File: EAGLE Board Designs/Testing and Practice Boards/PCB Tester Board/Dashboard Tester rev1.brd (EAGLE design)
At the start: 160 x 100 mm, 26 parts, among them J1 CONNECTOR-CAN_NF_T_V_BLACK, J2 CONNECTOR-6_NF_T_V_BLACK, J3 CONNECTOR-8_NF_T_V_BLACK, Q1 TRANSISTOR_N_MOS_PMV15ENEA, Q10 TRANSISTOR_N_MOS_PMV15ENEA, Q11 TRANSISTOR_P_MOS_SOT23_SI2369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, Q2 TRANSISTOR_N_MOS_PMV15ENEA, Q3 TRANSISTOR_N_MOS_PMV15ENEA, Q4 TRANSISTOR_N_MOS_PMV15ENEA, Q5 TRANSISTOR_N_MOS_PMV15ENEA, Q6 TRANSISTOR_N_MOS_PMV15ENEA, Q7 TRANSISTOR_P_MOS_SOT23_SI2369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, Q8 TRANSISTOR_N_MOS_PMV15ENEA, Q9 TRANSISTOR_P_MOS_SOT23_SI2369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, U1 TEENSY_3.5, U2 CAN_TRANSCIEVER_TCAN1051HQV-Q1, U3 VOLTAGE_REGULATOR__5V

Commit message: Merge in master to update files
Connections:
- net VIO renamed +3V3
- removed net IN: U3.1
- removed net OUT: U3.3
- removed net VDD: U2.3
- removed net VIN: U1.VIN
- new net +5V: U1.VIN, U2.3, U3.3
- new net CANH: J1.4, U2.7
- new net CANL: J1.3, U2.6
- new net N$20: U1.D3, U2.1
- new net N$23: U1.D4, U2.4
- net +12V: now also U3.1
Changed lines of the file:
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@@
 </elements>
 <signals>
-<signal name="VIN">
-<contactref element="U1" pad="VIN"/>
-</signal>
 <signal name="AGND">
 <contactref element="U1" pad="AGND/GND"/>
@@
 <wire x1="-57.13" y1="6.35" x2="-30.48" y2="38.1" width="0" layer="19" extent="1-1"/>
 </signal>
-<signal name="VDD">
-<contactref element="U2" pad="3"/>
-</signal>
-<signal name="VIO">
-<contactref element="U2" pad="5"/>
-</signal>
-<signal name="IN">
-<contactref element="U3" pad="1"/>
-</signal>
-<signal name="OUT">
-<contactref element="U3" pad="3"/>
-</signal>
 <signal name="+12V">
 <contactref element="J1" pad="1"/>
@@
 <contactref element="RN6" pad="7"/>
 <contactref element="DN3" pad="3"/>
+<contactref element="U3" pad="1"/>
 <wire x1="-23.48" y1="80.33" x2="-24.8031" y2="80.33" width="0" layer="19" extent="1-1"/>
 <wire x1="-18.1102" y1="75.1967" x2="-23.48" y2="80.33" width="0" layer="19" extent="1-1"/>
+<wire x1="-21.59" y1="67.31" x2="-18.1102" y2="75.1967" width="0" layer="19" extent="1-1"/>
 <wire x1="-56.28" y1="77.1" x2="-24.8031" y2="80.33" width="0" layer="19" extent="1-1"/>
 <wire x1="-57.08" y1="77.1" x2="-56.28" y2="77.1" width="0" layer="19" extent="1-1"/>
@@
 <contactref element="Q11" pad="3"/>
 </signal>
+<signal name="+5V">
+<contactref element="U2" pad="3"/>
+<contactref element="U3" pad="3"/>
+<contactref element="U1" pad="VIN"/>
+<wire x1="-27.305" y1="63.4365" x2="-16.51" y2="67.31" width="0" layer="19" extent="1-1"/>
+<wire x1="-30.48" y1="2.54" x2="-27.305" y2="63.4365" width="0" layer="19" extent="1-1"/>
+</signal>
+<signal name="+3V3">
+<contactref element="U2" pad="5"/>
+</signal>
+<signal name="CANH">
+<contactref element="J1" pad="4"/>
+<contactref element="U2" pad="7"/>
+<wire x1="-28.575" y1="68.6435" x2="-57.13" y2="3.85" width="0" layer="19" extent="1-1"/>
+</signal>
+<signal name="CANL">
+<contactref element="J1" pad="3"/>
+<contactref element="U2" pad="6"/>
+<wire x1="-27.305" y1="68.6435" x2="-54.63" y2="3.85" width="0" layer="19" extent="1-1"/>
+</signal>
+<signal name="N$20">
+<contactref element="U2" pad="1"/>
+<contactref element="U1" pad="D3"/>
+<wire x1="-15.24" y1="12.7" x2="-29.845" y2="63.4365" width="0" layer="19" extent="1-1"/>
+</signal>
+<signal name="N$23">
+<contactref element="U1" pad="D4"/>
+<contactref element="U2" pad="4"/>
+<wire x1="-15.24" y1="15.24" x2="-26.035" y2="63.4365" width="0" layer="19" extent="1-1"/>
+</signal>
 </signals>

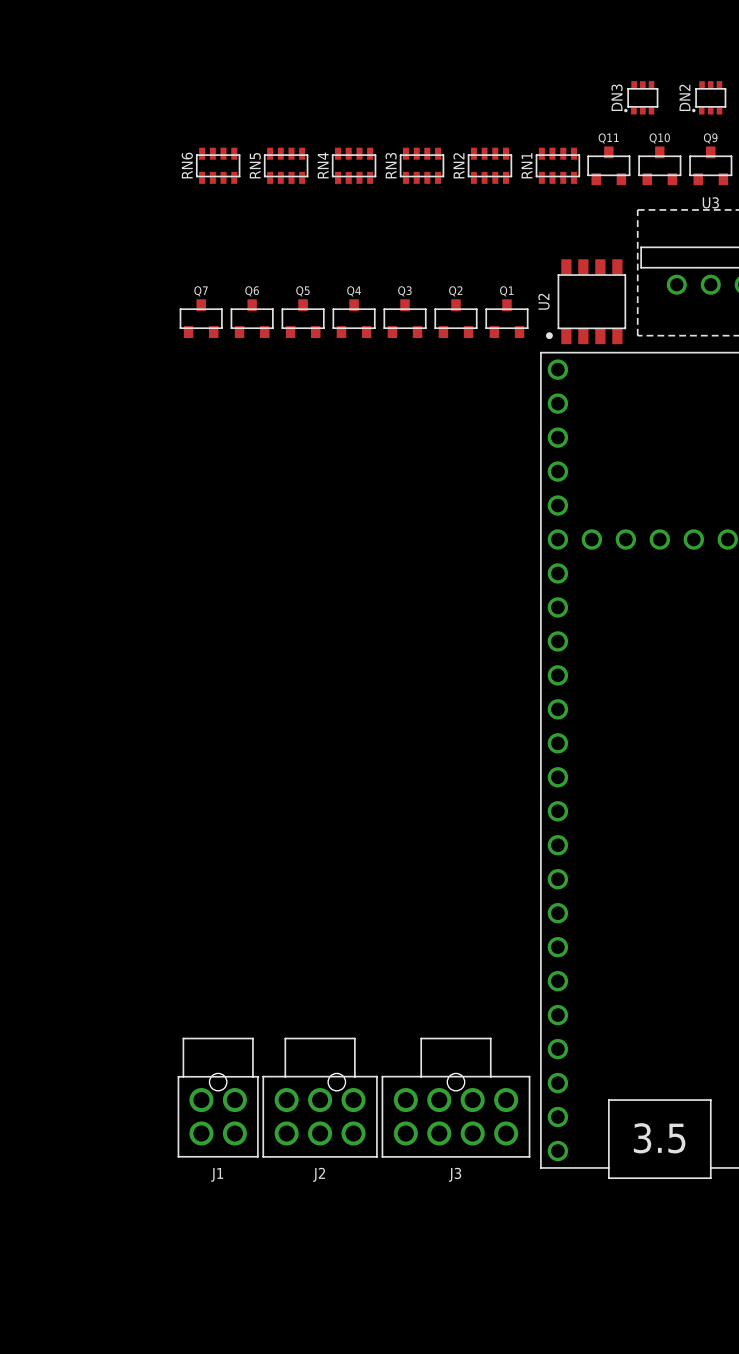
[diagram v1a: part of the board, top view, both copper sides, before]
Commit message: Ready to route except for connections to teensy
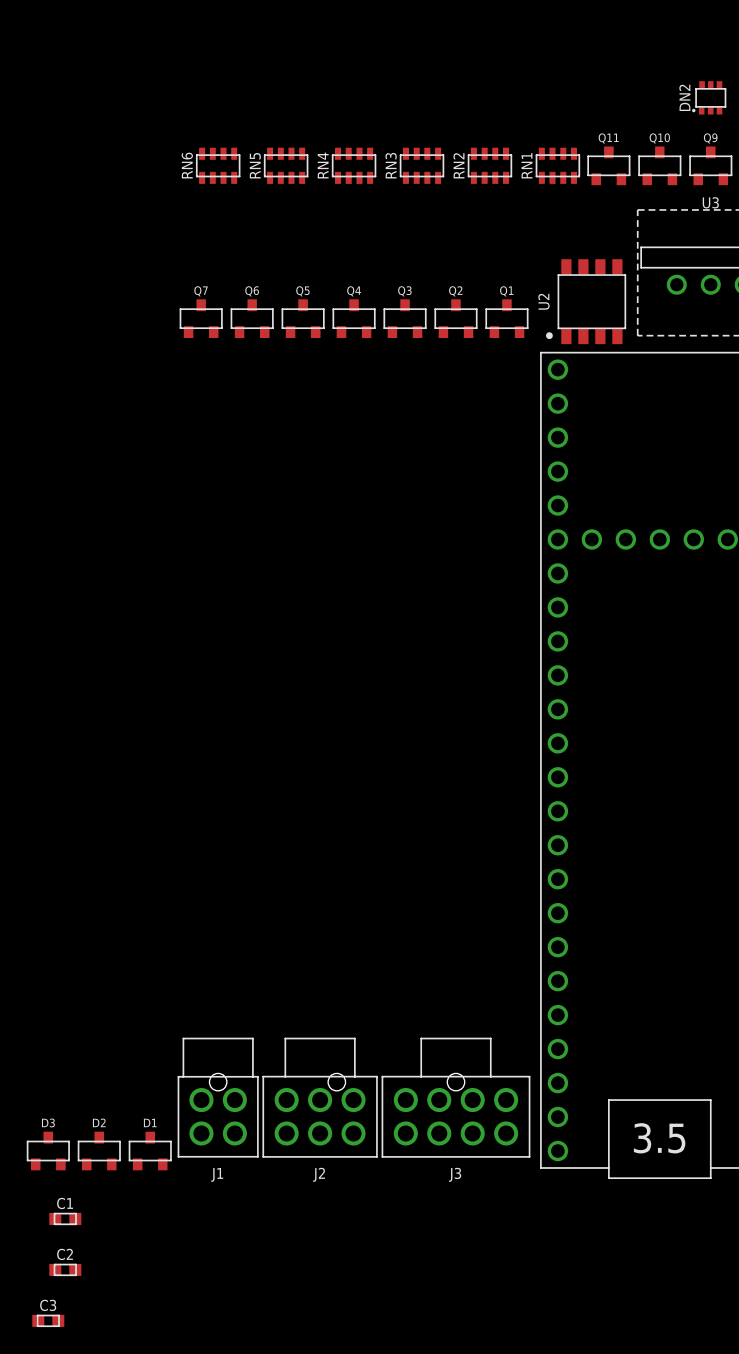
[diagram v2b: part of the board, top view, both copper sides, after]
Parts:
- removed DN3: TVS_ARRAY_16V, HyTechDevices:SOT363
- added C1: CAPACITOR_0603_25V_1UF, HyTechDevices:0603-CAP
- added C2, C3: CAPACITOR_0603_10V_1UF, HyTechDevices:0603-CAP
- added D1, D2, D3: TVS_15V, HyTechDevices:SOT-23
- U3: value VOLTAGE_REGULATOR__5V -> VOLTAGE_REGULATOR_OKI-78SR_5V
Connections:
- net N$11 renamed BTN_LC_CTRL
- net N$2 renamed BTN_MARK_CTRL
- net N$5 renamed BTN_MC_CYCLE_CTRL
- net N$7 renamed BTN_MODE_CTRL
- net N$9 renamed BTN_START_CTRL
- removed net N$25: Q5.3
- removed net N$26: Q4.3
- removed net N$27: Q3.3
- removed net N$28: Q2.3
- removed net N$29: Q1.3
- new net BTN_LAUNCH_CONTROL: J3.7, Q5.3
- new net BTN_MARK: J3.2, Q1.3
- new net BTN_MC_CYCLE: J3.3, Q2.3
- new net BTN_MODE: J3.5, Q3.3
- new net BTN_START: J3.6, Q4.3
- new net BUZZER_CTRL: J3.4
- net +12V: now also C1.1, D1.3, D2.3; no longer DN3.1, DN3.3
- net +5V: now also C2.1, C3.2
- net CANH: now also J2.5
- net CANL: now also J2.4
- net DASH_12V: now also J2.1
- net GND: now also C1.2, C2.2, C3.1, J2.2
- net N$16: now also D2.1
- net N$19: now also D1.1; no longer DN3.2
- net N$22: now also D3.1
- net SHUTDOWN_H_OUT: now also J2.6
- net SSOK_OUT: now also D3.3, J2.3; no longer DN3.4

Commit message: Control connections to teensy
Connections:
- new net N$5: U1.D36
- net BTN_LC_CTRL: now also U1.D35
- net BTN_MARK_CTRL: now also U1.D31
- net BTN_MC_CYCLE_CTRL: now also U1.D32
- net BTN_MODE_CTRL: now also U1.D33
- net BTN_START_CTRL: now also U1.D34
- net SHUTDOWN_H_CTRL: now also U1.D38
- net SSOK_CTRL: now also U1.D37
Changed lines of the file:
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@@
 <contactref element="DN1" pad="1"/>
 <contactref element="RN2" pad="8"/>
+<contactref element="U1" pad="D31"/>
 <wire x1="-31.68" y1="75.3" x2="-14.6431" y2="80.33" width="0" layer="19" extent="1-1"/>
 <wire x1="-36.76" y1="77.1" x2="-31.68" y2="75.3" width="0" layer="19" extent="1-1"/>
+<wire x1="-15.24" y1="58.42" x2="-14.6431" y2="80.33" width="0" layer="19" extent="1-1"/>
 </signal>
 <signal name="N$4">
@@
 <contactref element="RN2" pad="7"/>
 <contactref element="DN1" pad="3"/>
+<contactref element="U1" pad="D32"/>
 <wire x1="-30.88" y1="75.3" x2="-13.32" y2="80.33" width="0" layer="19" extent="1-1"/>
 <wire x1="-35.96" y1="77.1" x2="-30.88" y2="75.3" width="0" layer="19" extent="1-1"/>
+<wire x1="-15.24" y1="60.96" x2="-13.32" y2="80.33" width="0" layer="19" extent="1-1"/>
 </signal>
 <signal name="N$6">
@@
 <contactref element="RN2" pad="6"/>
 <contactref element="DN1" pad="4"/>
+<contactref element="U1" pad="D33"/>
 <wire x1="-30.08" y1="75.3" x2="-13.32" y2="82.23" width="0" layer="19" extent="1-1"/>
 <wire x1="-35.16" y1="77.1" x2="-30.08" y2="75.3" width="0" layer="19" extent="1-1"/>
+<wire x1="-30.48" y1="60.96" x2="-30.08" y2="75.3" width="0" layer="19" extent="1-1"/>
 </signal>
 <signal name="N$8">
@@
 <contactref element="RN2" pad="5"/>
 <contactref element="DN1" pad="5"/>
+<contactref element="U1" pad="D34"/>
 <wire x1="-29.28" y1="75.3" x2="-13.97" y2="82.23" width="0" layer="19" extent="1-1"/>
 <wire x1="-34.36" y1="77.1" x2="-29.28" y2="75.3" width="0" layer="19" extent="1-1"/>
+<wire x1="-30.48" y1="58.42" x2="-29.28" y2="75.3" width="0" layer="19" extent="1-1"/>
 </signal>
 <signal name="N$10">
@@
 <contactref element="RN4" pad="8"/>
 <contactref element="DN1" pad="6"/>
+<contactref element="U1" pad="D35"/>
 <wire x1="-41.84" y1="75.3" x2="-14.62" y2="82.23" width="0" layer="19" extent="1-1"/>
 <wire x1="-46.92" y1="77.1" x2="-41.84" y2="75.3" width="0" layer="19" extent="1-1"/>
+<wire x1="-30.48" y1="55.88" x2="-41.84" y2="75.3" width="0" layer="19" extent="1-1"/>
 </signal>
 <signal name="N$3">
@@
 <contactref element="RN4" pad="6"/>
 <contactref element="DN2" pad="3"/>
+<contactref element="U1" pad="D37"/>
 <wire x1="-40.24" y1="75.3" x2="-18.4" y2="80.33" width="0" layer="19" extent="1-1"/>
 <wire x1="-45.32" y1="77.1" x2="-40.24" y2="75.3" width="0" layer="19" extent="1-1"/>
+<wire x1="-30.48" y1="50.8" x2="-40.24" y2="75.3" width="0" layer="19" extent="1-1"/>
 </signal>
 <signal name="N$15">
@@
 <contactref element="RN4" pad="5"/>
 <contactref element="DN2" pad="4"/>
+<contactref element="U1" pad="D38"/>
 <wire x1="-39.44" y1="75.3" x2="-18.4" y2="82.23" width="0" layer="19" extent="1-1"/>
 <wire x1="-44.52" y1="77.1" x2="-39.44" y2="75.3" width="0" layer="19" extent="1-1"/>
+<wire x1="-30.48" y1="48.26" x2="-39.44" y2="75.3" width="0" layer="19" extent="1-1"/>
 </signal>
 <signal name="N$21">
@@
 <wire x1="-15.24" y1="12.7" x2="-29.845" y2="63.4365" width="0" layer="19" extent="1-1"/>
 </signal>
-<signal name="N$23">
-<contactref element="U1" pad="D4"/>
-<contactref element="U2" pad="4"/>
-<wire x1="-15.24" y1="15.24" x2="-26.035" y2="63.4365" width="0" layer="19" extent="1-1"/>
-</signal>
 <signal name="BTN_MARK">
 <contactref element="J3" pad="2"/>
@@
 <wire x1="-49.53" y1="65.7733" x2="-39.35" y2="3.85" width="0" layer="19" extent="1-1"/>
 </signal>
+<signal name="N$2">
+<contactref element="U1" pad="D4"/>
+<contactref element="U2" pad="4"/>
+<wire x1="-15.24" y1="15.24" x2="-26.035" y2="63.4365" width="0" layer="19" extent="1-1"/>
+</signal>
+<signal name="N$5">
+<contactref element="U1" pad="D36"/>
+</signal>
 </signals>

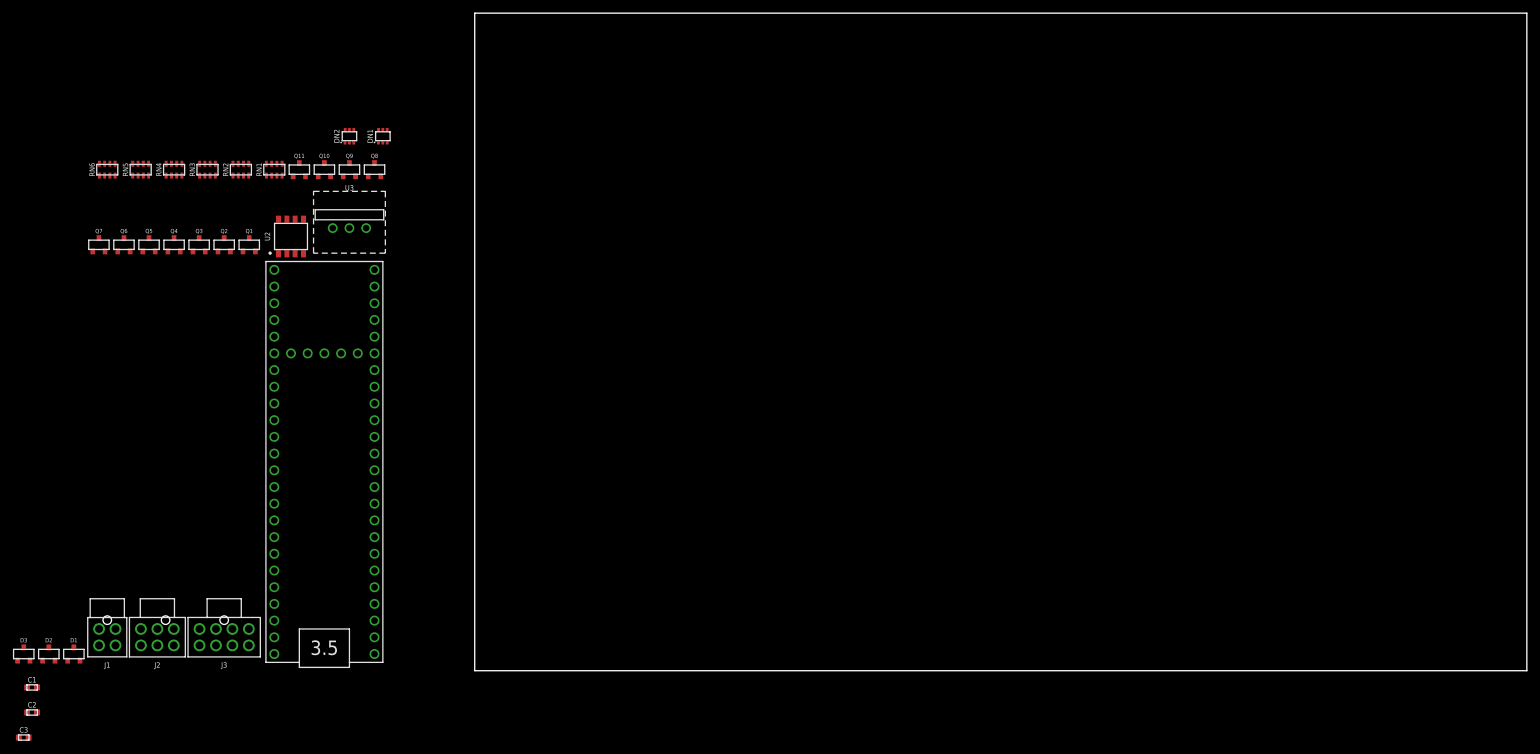
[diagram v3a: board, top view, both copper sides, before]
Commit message: Connected buzzer, began tracing
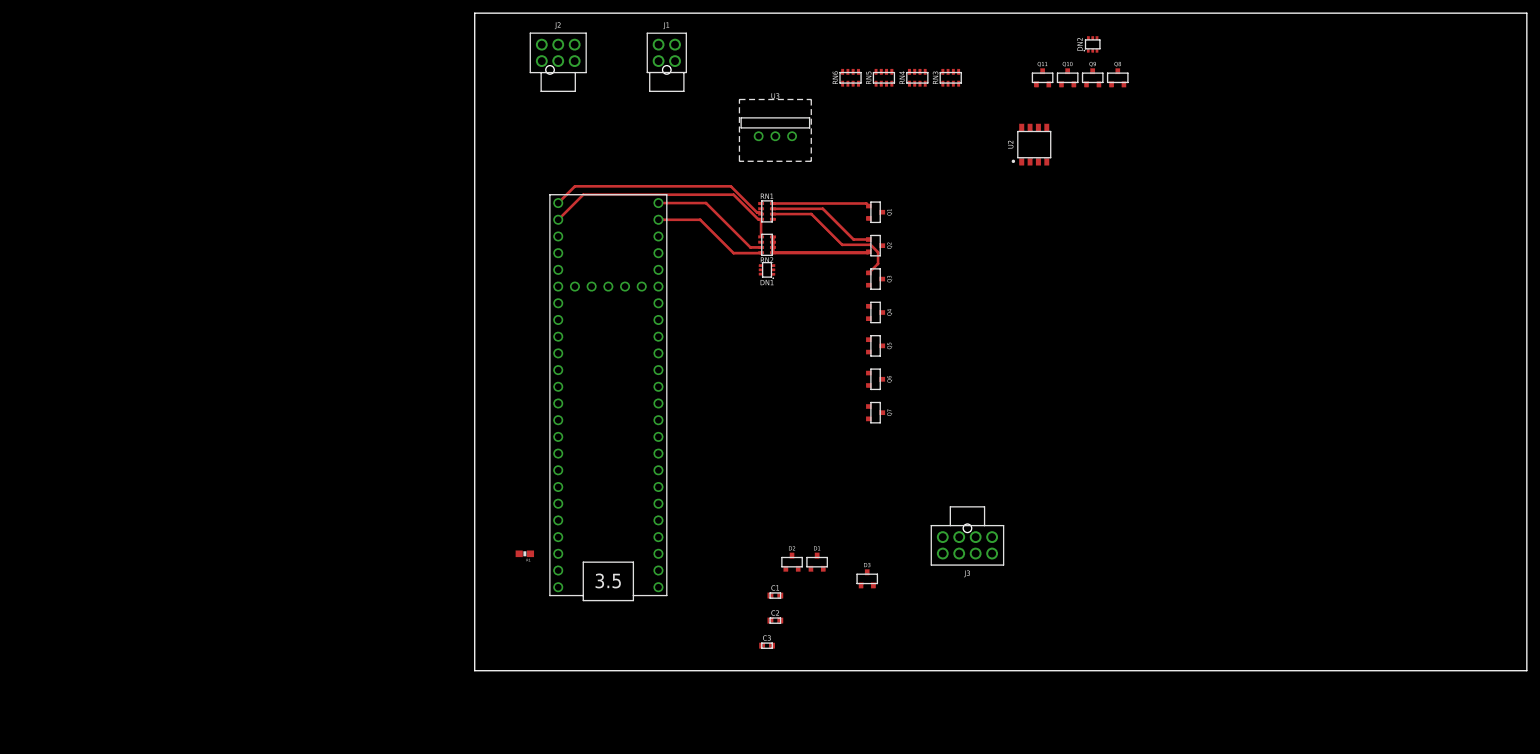
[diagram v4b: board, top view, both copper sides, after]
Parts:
- added R1: 1k, HyTechDevices:0603-RES
- moved D3 128.8 mm to (59.7, 14.0)
- moved J1 121.2 mm to (29.2, 92.7), turned to 180 degrees
- moved Q7 120.8 mm to (61.0, 39.2), turned to 270 degrees
- moved Q6 116.1 mm to (61.0, 44.3), turned to 270 degrees
- moved C1 113.9 mm to (45.7, 11.4)
- moved C2 113.9 mm to (45.7, 7.62)
- moved C3 113.9 mm to (44.5, 3.81)
- moved D1 113.9 mm to (52.1, 16.5)
- moved D2 113.9 mm to (48.3, 16.5)
- moved DN2 113.9 mm to (94.0, 95.2)
- moved J3 113.9 mm to (74.9, 20.3)
- moved Q10 113.9 mm to (90.2, 90.2)
- moved Q11 113.9 mm to (86.4, 90.2)
- moved Q8 113.9 mm to (97.8, 90.2)
- moved Q9 113.9 mm to (94.0, 90.2)
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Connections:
- removed net 3.3V: U1.3V3, U1.3V3@2, U1.3V3@3
- new net N$7: R1.1, U1.3V3, U1.3V3@2, U1.3V3@3
- new net N$9: R1.2
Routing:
- net BTN_START_CTRL: track 0.00 -> 36.7 mm
- net BTN_MODE_CTRL: track 0.00 -> 33.6 mm
- net N$6: track 0.00 -> 22.1 mm
- net BTN_MC_CYCLE_CTRL: track 0.00 -> 18.4 mm
- net BTN_MARK_CTRL: track 0.00 -> 17.7 mm
- net GND: track 0.00 -> 17.1 mm
- net N$4: track 0.00 -> 16.5 mm
- net N$1: track 0.00 -> 14.8 mm
